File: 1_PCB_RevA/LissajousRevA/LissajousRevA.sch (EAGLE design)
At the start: 87 parts, among them U101 LM348D, U201 LM348D, U401 LM348D

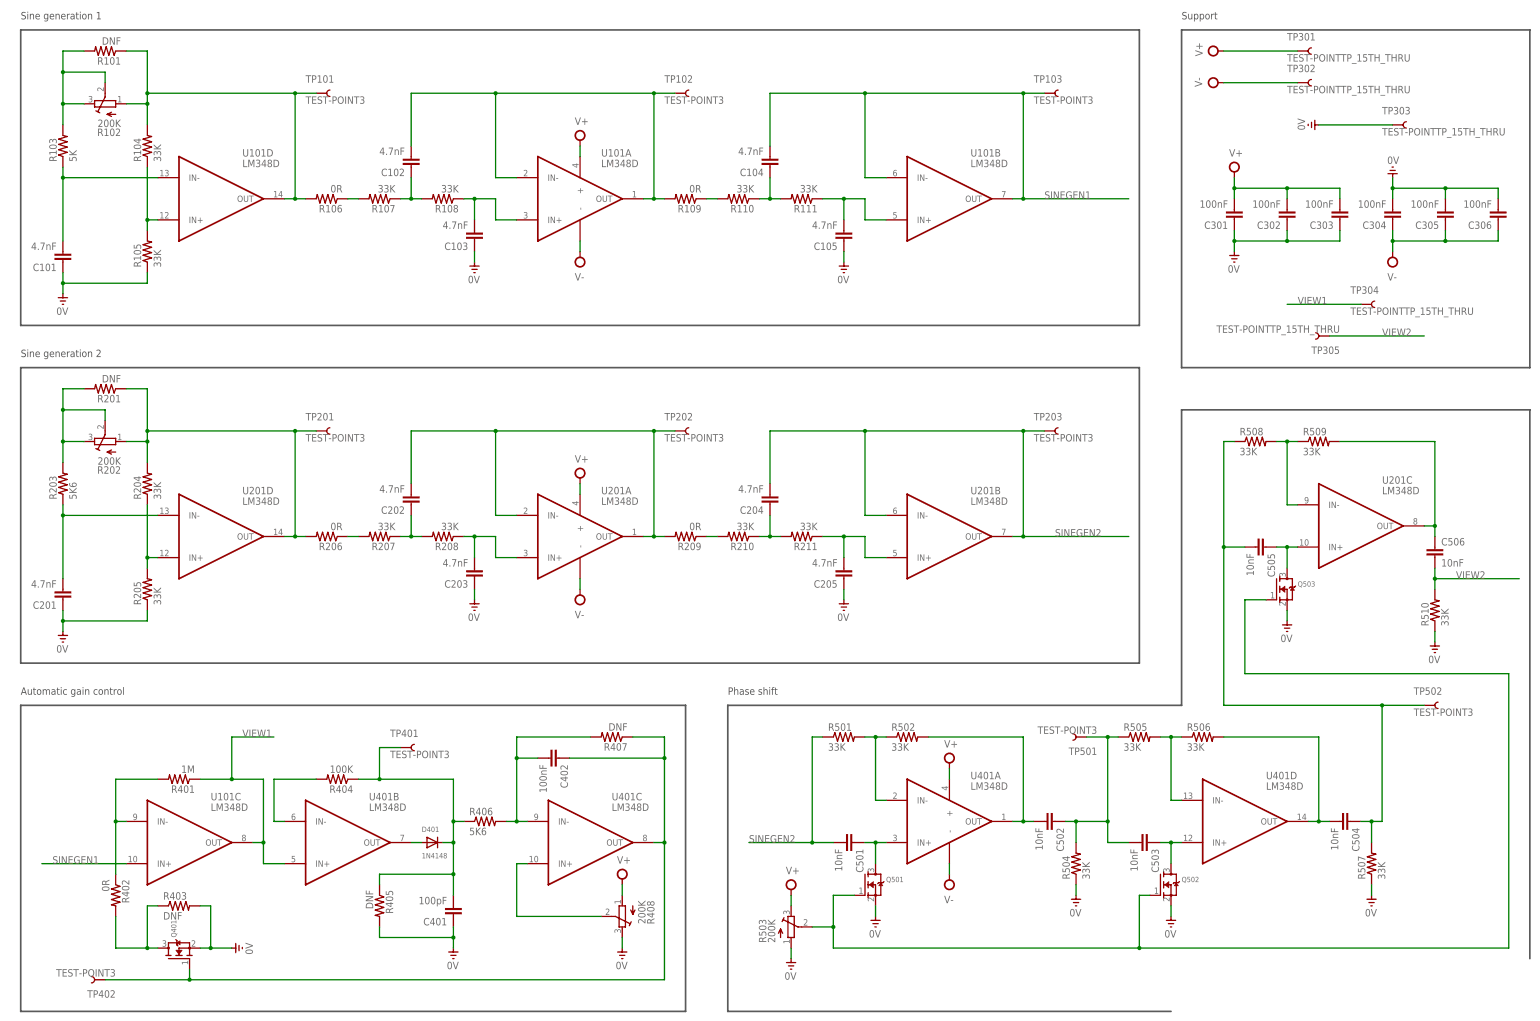
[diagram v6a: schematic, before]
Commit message: removed test points, can just use legs instead
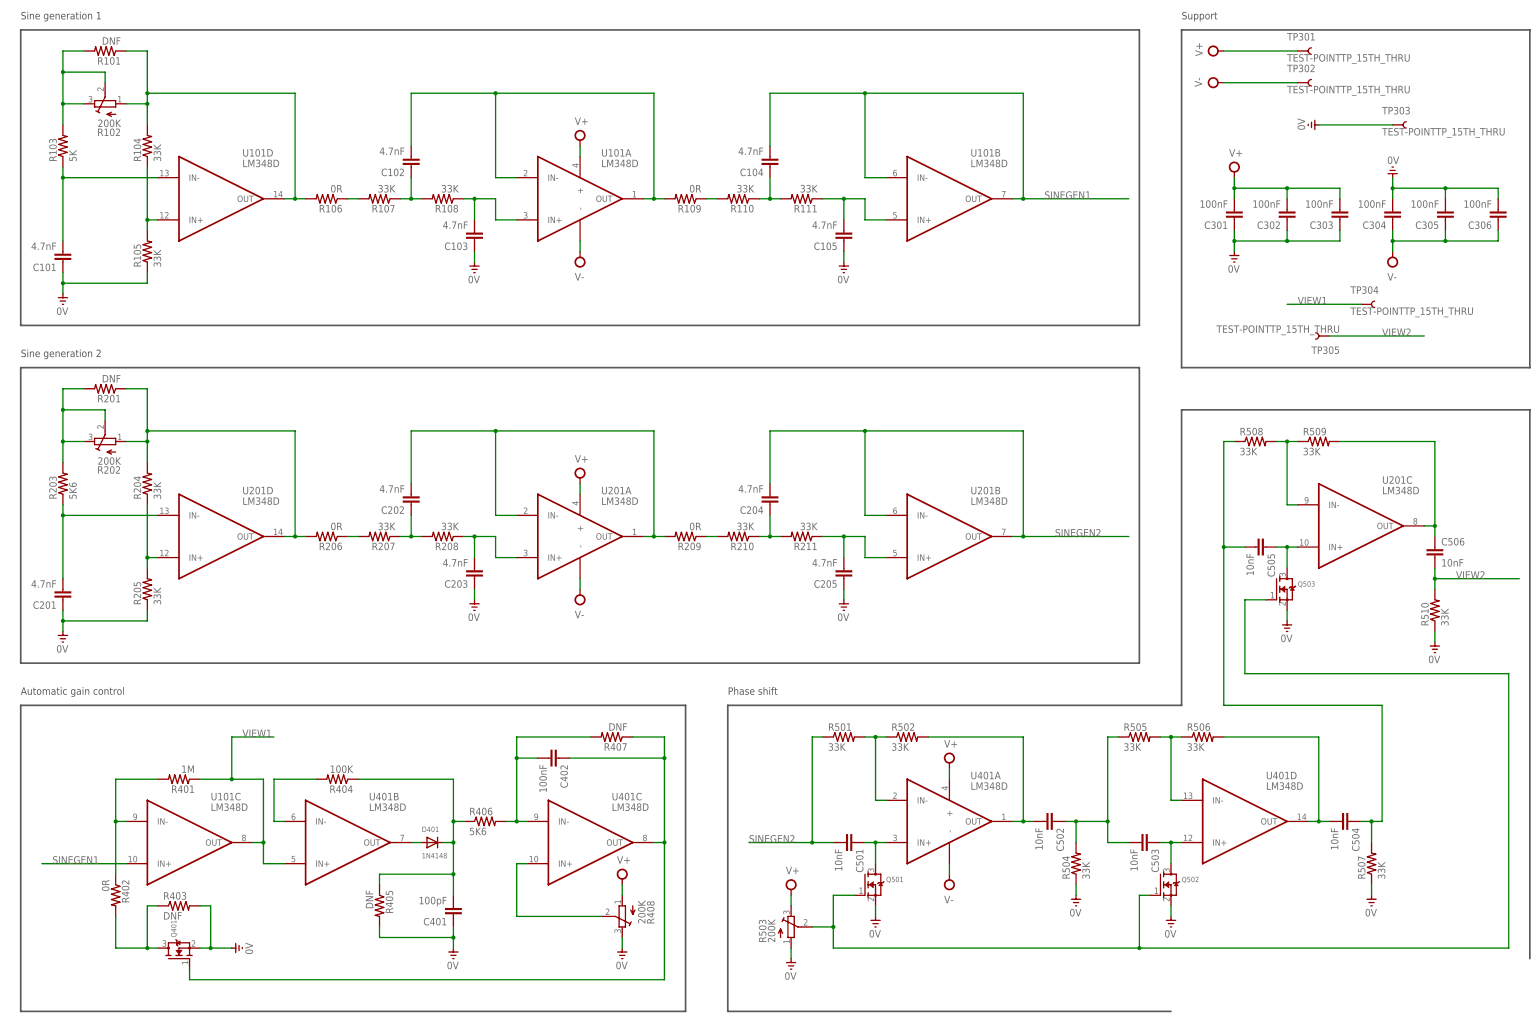
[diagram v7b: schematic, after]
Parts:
- removed TP101, TP102, TP103, TP201, TP202, TP203, TP401, TP402, TP501, TP502: TEST-POINT3, passives:TEST-POINT3
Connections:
- net N$15: no longer TP201.1
- net N$21: no longer TP202.1
- net N$29: no longer TP501.1
- net N$30: no longer TP401.1
- net N$32: no longer TP402.1
- net N$42: no longer TP502.1
- net N$7: no longer TP101.1
- net N$8: no longer TP102.1
- net SINEGEN1: no longer TP103.1
- net SINEGEN2: no longer TP203.1
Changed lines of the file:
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@@
 <part name="R106" library="passives" deviceset="RESISTOR" device="0603-RES" value="0R"/>
 <part name="R109" library="passives" deviceset="RESISTOR" device="0603-RES" value="0R"/>
-<part name="TP101" library="passives" deviceset="TEST-POINT" device="3"/>
-<part name="TP102" library="passives" deviceset="TEST-POINT" device="3"/>
-<part name="TP103" library="passives" deviceset="TEST-POINT" device="3"/>
 <part name="U201" library="LM348D" deviceset="LM348D" device=""/>
 <part name="R205" library="passives" deviceset="RESISTOR" device="0603-RES" value="33K"/>
@@
 <part name="R206" library="passives" deviceset="RESISTOR" device="0603-RES" value="0R"/>
 <part name="R209" library="passives" deviceset="RESISTOR" device="0603-RES" value="0R"/>
-<part name="TP201" library="passives" deviceset="TEST-POINT" device="3"/>
-<part name="TP202" library="passives" deviceset="TEST-POINT" device="3"/>
-<part name="TP203" library="passives" deviceset="TEST-POINT" device="3"/>
 <part name="TP301" library="passives" deviceset="TEST-POINT" device="TP_15TH_THRU"/>
 <part name="TP303" library="passives" deviceset="TEST-POINT" device="TP_15TH_THRU"/>
@@
 <part name="R402" library="passives" deviceset="RESISTOR" device="0603-RES" value="0R"/>
 <part name="R403" library="passives" deviceset="RESISTOR" device="0603-RES" value="DNF"/>
-<part name="TP401" library="passives" deviceset="TEST-POINT" device="3"/>
-<part name="TP402" library="passives" deviceset="TEST-POINT" device="3"/>
 <part name="V22" library="supply" deviceset="V+" device=""/>
 <part name="V23" library="supply" deviceset="V-" device=""/>
@@
 <part name="R510" library="passives" deviceset="RESISTOR" device="0603-RES" value="33K"/>
 <part name="V31" library="supply" deviceset="0V" device=""/>
-<part name="TP501" library="passives" deviceset="TEST-POINT" device="3"/>
-<part name="TP502" library="passives" deviceset="TEST-POINT" device="3"/>
 <part name="TP305" library="passives" deviceset="TEST-POINT" device="TP_15TH_THRU"/>
 <part name="TP304" library="passives" deviceset="TEST-POINT" device="TP_15TH_THRU"/>
@@
 <instance part="R106" gate="G$1" x="83.82" y="208.28" rot="R180"/>
 <instance part="R109" gate="G$1" x="170.18" y="208.28" rot="R180"/>
-<instance part="TP101" gate="G$1" x="81.28" y="233.68"/>
-<instance part="TP102" gate="G$1" x="167.64" y="233.68"/>
-<instance part="TP103" gate="G$1" x="256.54" y="233.68"/>
 <instance part="U201" gate="A" x="129.54" y="121.92"/>
 <instance part="U201" gate="B" x="218.44" y="127"/>
@@
 <instance part="R206" gate="G$1" x="83.82" y="127" rot="R180"/>
 <instance part="R209" gate="G$1" x="170.18" y="127" rot="R180"/>
-<instance part="TP201" gate="G$1" x="81.28" y="152.4"/>
-<instance part="TP202" gate="G$1" x="167.64" y="152.4"/>
-<instance part="TP203" gate="G$1" x="256.54" y="152.4"/>
 <instance part="TP301" gate="G$1" x="317.5" y="243.84"/>
 <instance part="TP303" gate="G$1" x="340.36" y="226.06"/>
@@
 <instance part="R402" gate="G$1" x="33.02" y="40.64" rot="R270"/>
 <instance part="R403" gate="G$1" x="48.26" y="38.1"/>
-<instance part="TP401" gate="G$1" x="101.6" y="76.2"/>
-<instance part="TP402" gate="G$1" x="30.48" y="20.32" rot="R180"/>
 <instance part="V22" gate="1" x="233.68" y="73.66"/>
 <instance part="V23" gate="1" x="233.68" y="43.18"/>
@@
 <instance part="R510" gate="G$1" x="350.52" y="109.22" rot="R90"/>
 <instance part="V31" gate="1" x="350.52" y="99.06"/>
-<instance part="TP501" gate="G$1" x="266.7" y="78.74" rot="R180"/>
-<instance part="TP502" gate="G$1" x="347.98" y="86.36"/>
 <instance part="TP305" gate="G$1" x="325.12" y="175.26" rot="R180"/>
 <instance part="TP304" gate="G$1" x="332.74" y="182.88"/>
@@
 <wire x1="76.2" y1="233.68" x2="40.64" y2="233.68" width="0.1524" layer="91"/>
 <junction x="40.64" y="233.68"/>
-<pinref part="TP101" gate="G$1" pin="1"/>
-<wire x1="81.28" y1="233.68" x2="76.2" y2="233.68" width="0.1524" layer="91"/>
-<junction x="76.2" y="233.68"/>
 </segment>
 </net>
@@
 <wire x1="162.56" y1="208.28" x2="165.1" y2="208.28" width="0.1524" layer="91"/>
 <junction x="162.56" y="208.28"/>
-<pinref part="TP102" gate="G$1" pin="1"/>
-<wire x1="167.64" y1="233.68" x2="162.56" y2="233.68" width="0.1524" layer="91"/>
-<junction x="162.56" y="233.68"/>
 </segment>
 </net>
@@
 <wire x1="76.2" y1="152.4" x2="40.64" y2="152.4" width="0.1524" layer="91"/>
 <junction x="40.64" y="152.4"/>
-<pinref part="TP201" gate="G$1" pin="1"/>
-<wire x1="81.28" y1="152.4" x2="76.2" y2="152.4" width="0.1524" layer="91"/>
-<junction x="76.2" y="152.4"/>
 </segment>
 </net>
@@
 <pinref part="U201" gate="B" pin="OUT"/>
 <wire x1="248.92" y1="127" x2="251.46" y2="127" width="0.1524" layer="91"/>
-<pinref part="TP203" gate="G$1" pin="1"/>
-<wire x1="256.54" y1="152.4" x2="251.46" y2="152.4" width="0.1524" layer="91"/>
-<junction x="251.46" y="152.4"/>
 <wire x1="251.46" y1="127" x2="276.86" y2="127" width="0.1524" layer="91"/>
 <junction x="251.46" y="127"/>
@@
 <wire x1="162.56" y1="127" x2="165.1" y2="127" width="0.1524" layer="91"/>
 <junction x="162.56" y="127"/>
-<pinref part="TP202" gate="G$1" pin="1"/>
-<wire x1="167.64" y1="152.4" x2="162.56" y2="152.4" width="0.1524" layer="91"/>
-<junction x="162.56" y="152.4"/>
 </segment>
 </net>
@@
 <pinref part="U101" gate="B" pin="OUT"/>
 <wire x1="248.92" y1="208.28" x2="251.46" y2="208.28" width="0.1524" layer="91"/>
-<pinref part="TP103" gate="G$1" pin="1"/>
-<wire x1="256.54" y1="233.68" x2="251.46" y2="233.68" width="0.1524" layer="91"/>
-<junction x="251.46" y="233.68"/>
 <wire x1="251.46" y1="208.28" x2="276.86" y2="208.28" width="0.1524" layer="91"/>
 <junction x="251.46" y="208.28"/>
@@
 <wire x1="165.1" y1="20.32" x2="165.1" y2="53.34" width="0.1524" layer="91"/>
 <junction x="165.1" y="53.34"/>
-<pinref part="TP402" gate="G$1" pin="1"/>
-<wire x1="30.48" y1="20.32" x2="50.8" y2="20.32" width="0.1524" layer="91"/>
-<junction x="50.8" y="20.32"/>
 </segment>
 </net>
@@
 <wire x1="114.3" y1="53.34" x2="114.3" y2="58.42" width="0.1524" layer="91"/>
 <wire x1="114.3" y1="58.42" x2="114.3" y2="68.58" width="0.1524" layer="91"/>
-<wire x1="114.3" y1="68.58" x2="96.52" y2="68.58" width="0.1524" layer="91"/>
+<wire x1="114.3" y1="68.58" x2="91.44" y2="68.58" width="0.1524" layer="91"/>
 <pinref part="C401" gate="G$1" pin="2"/>
-<wire x1="96.52" y1="68.58" x2="91.44" y2="68.58" width="0.1524" layer="91"/>
 <wire x1="114.3" y1="40.64" x2="114.3" y2="45.72" width="0.1524" layer="91"/>
 <junction x="114.3" y="53.34"/>
@@
 <wire x1="116.84" y1="58.42" x2="114.3" y2="58.42" width="0.1524" layer="91"/>
 <junction x="114.3" y="58.42"/>
-<pinref part="TP401" gate="G$1" pin="1"/>
-<wire x1="101.6" y1="76.2" x2="96.52" y2="76.2" width="0.1524" layer="91"/>
-<wire x1="96.52" y1="76.2" x2="96.52" y2="68.58" width="0.1524" layer="91"/>
-<junction x="96.52" y="68.58"/>
 </segment>
 </net>
@@
 <junction x="264.16" y="58.42"/>
 <junction x="271.78" y="58.42"/>
-<pinref part="TP501" gate="G$1" pin="1"/>
-<wire x1="271.78" y1="78.74" x2="266.7" y2="78.74" width="0.1524" layer="91"/>
-<junction x="271.78" y="78.74"/>
 </segment>
 </net>
@@
 <wire x1="299.72" y1="124.46" x2="299.72" y2="149.86" width="0.1524" layer="91"/>
 <junction x="299.72" y="124.46"/>
-<pinref part="TP502" gate="G$1" pin="1"/>
-<wire x1="347.98" y1="86.36" x2="337.82" y2="86.36" width="0.1524" layer="91"/>
-<junction x="337.82" y="86.36"/>
-</segment>
-</net>
+</segment>
+</net>
